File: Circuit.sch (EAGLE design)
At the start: 120 parts, among them IC1 LM1117T-3.3-V, U1 MAG3110, U10 MMA8452Q, U11 MMA8452Q, U12 MMA8452Q, U2 MAG3110, U3 L3G4200D, U4 L3G4200D, U5 L3G4200D, U6 L3G4200D, U7 MMA8452Q, U8 MMA8452Q, U9 MMA8452Q

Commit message: Corrected erc violations
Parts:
- C12, C7: value 4.7uF -> 10nF
- C15: value 2.2nF -> 470nF
- C16, C18, C43: value 0.1uF -> 2.2nF
- C17, C45: value 10nF -> 2.2nF
- C19, C2, C26, C33: value 4.7uF -> 0.1uF
- C22: value 2.2nF -> 4.7uF
- C23, C51: value 0.1uF -> 4.7uF
- C24, C49: value 10nF -> 4.7uF
- C29, C36, C9: value 2.2nF -> 10uF
- C30, C34, C35, C39, C57, C8: value 0.1uF -> 10nF
- C31: value 10nF -> 470nF
- C38, C41, C53: value 10nF -> 0.1uF
- C4: value 2.2nF -> 0.1uF
- C40, C48, C52: value 10uF -> 0.1uF
- C44: value 10uF -> 2.2nF
- C46, C54: value 470nF -> 0.1uF
- C50: value 470nF -> 4.7uF
- C56: value 0.1uF -> 10uF
- C58: value 0.1uF -> 470nF
- R1, R11, R2, R22, R26, R38: value 2.2K -> 10K
- R15, R18, R21, R24, R29, R30: value 10K -> 2.2K
- U$1: value RASPBERRY-PI_REV2 -> PCA9546A; device RaspberryPi:RASPBERRY-PI_REV2 -> Gyros:PCA9546A
- U$3: value PCA9546A -> RASPBERRY-PI_REV2; device Gyros:PCA9546A -> RaspberryPi:RASPBERRY-PI_REV2
- U12, U7, U8: value MMA8452Q -> L3G4200D; device SparkFun:MMA8452Q -> SparkFun:L3G4200D
- U4, U5, U6: value L3G4200D -> MMA8452Q; device SparkFun:L3G4200D -> SparkFun:MMA8452Q
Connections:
- net +3V3: now also C13.1, C14.1, C20.1, C21.1, C22.1, C29.1, C34.1, C35.1, C36.1, C46.1, C49.1, C5.1, C50.1, C56.1, C8.1, C9.1, ITG2.AD0, R1.1, R10.1, R12.1, R14.2, R15.2, R16.2, R17.2, R18.2, R19.2, R2.1, R21.1, R24.1, R25.1, R27.1, R28.1, R30.2, R31.2, R32.2, R35.2, R39.2, R40.2, R7.1, R8.1, R9.1, U$1.A2, U$1.VCC, U12.CS, U12.RSVDV@0, U12.SDO, U7.CS, U7.RSVDV@0, U7.SDO, U8.CS, U8.RSVDV@0; no longer C1.1, C11.1, C12.1, C15.2, C16.1, C16.2, C17.1, C18.1, C2.1, C22.2, C23.2, C26.1, C29.2, C30.1, C30.2, C31.1, C33.1, C38.1, C39.1, C43.1, C44.1, C6.1, ITG1.GND, ITG2.GND, ITG3.AD0, ITG3.GND, R1.2, R10.2, R11.2, R12.2, R14.1, R16.1, R17.1, R19.1, R2.2, R22.1, R25.2, R26.2, R27.2, R28.2, R30.1, R31.1, R32.1, R35.1, R38.1, R39.1, R40.1, R7.2, R8.2, R9.2, U$3.A2, U$3.VCC, U4.CS, U4.RSVDV@0, U4.SDO, U5.CS, U5.RSVDV@0, U6.CS, U6.RSVDV@0, U6.SDO
- net B1_SC0: now also R9.2, U$1.SC0; no longer R32.2, U$2.SC0
- net B1_SC1: now also ITG2.SCL, R8.2, U$1.SC1; no longer ITG3.SCL, R38.2, U$2.SC1
- net B1_SC2: now also R5.1, U$1.SC2, U7.SCL; no longer R28.1, U$2.SC2, U4.SCL
- net B1_SD0: now also R7.2, U$1.SD0; no longer R31.2, U$2.SD0
- net B1_SD1: now also ITG2.SDA, R10.2, R12.2, U$1.SD1; no longer ITG3.SDA, R14.2, R37.2, U$2.SD1
- net B1_SD2: now also R3.1, U$1.SD2, U7.SDA/SDI; no longer R27.1, U$2.SD2, U4.SDA/SDI
- net B2_SC0: now also ITG3.SCL, R28.2, U$2.SC0; no longer ITG2.SCL, R36.2, U$3.SC0
- net B2_SC1: now also R24.2, R29.2, U$2.SC1, U8.SCL; no longer R19.2, R40.2, U$3.SC1, U5.SCL
- net B2_SC2: now also R36.2, R6.1, U$2.SC2, U12.SCL; no longer R22.2, R26.1, U$3.SC2, U6.SCL
- net B2_SD0: now also ITG3.SDA, R23.2, U$2.SD0; no longer ITG2.SDA, R35.2, U$3.SD0
- net B2_SD1: now also R25.2, R27.2, U$2.SD1, U8.SDA/SDI; no longer R20.2, R39.2, U$3.SD1, U5.SDA/SDI
- net B2_SD2: now also R37.2, R4.1, U$2.SD2, U12.SDA/SDI; no longer R23.2, R25.1, U$3.SD2, U6.SDA/SDI
- net CLK1: now also R20.2, U$1.SCL, U$3.GPIO3,I2C0_SCL; no longer R16.2, U$1.GPIO3,I2C0_SCL, U$2.SCL
- net CLK2: now also U$2.SCL; no longer U$3.SCL
- net GND: now also C16.2, C22.2, C23.2, C29.2, C30.2, C46.2, C50.2, C54.2, ITG1.GND, ITG2.GND, ITG3.AD0, ITG3.GND, R11.1, R22.1, R26.1, R38.1, U$1.A0, U$1.A1, U$1.GND, U$3.GND@9, U12.GND, U12.RSDVG@3, U12.RSVDG@0, U12.RSVDG@1, U12.RSVDG@2, U12.RSVDG@4, U4.GND@0, U4.GND@1, U4.GND@2, U4.SA0, U5.GND@0, U5.GND@1, U5.GND@2, U5.SA0, U6.GND@0, U6.GND@1, U6.GND@2, U6.SA0, U7.GND, U7.RSDVG@3, U7.RSVDG@0, U7.RSVDG@1, U7.RSVDG@2, U7.RSVDG@4, U8.GND, U8.RSDVG@3, U8.RSVDG@0, U8.RSVDG@1, U8.RSVDG@2, U8.RSVDG@4, U8.SDO; no longer C31.2, C58.2, ITG2.AD0, R15.1, R18.1, R21.1, R24.1, U$1.GND@9, U$3.A0, U$3.A1, U$3.GND, U12.GND@0, U12.GND@1, U12.GND@2, U12.SA0, U4.GND, U4.RSDVG@3, U4.RSVDG@0, U4.RSVDG@1, U4.RSVDG@2, U4.RSVDG@4, U5.GND, U5.RSDVG@3, U5.RSVDG@0, U5.RSVDG@1, U5.RSVDG@2, U5.RSVDG@4, U5.SDO, U6.GND, U6.RSDVG@3, U6.RSVDG@0, U6.RSVDG@1, U6.RSVDG@2, U6.RSVDG@4, U7.GND@0, U7.GND@1, U7.GND@2, U7.SA0, U8.GND@0, U8.GND@1, U8.GND@2, U8.SA0
- net I1_AUXCLK: now also U5.SCL; no longer U7.SCL
- net I1_AUXSDA: now also U5.SDA; no longer U7.SDA
- net I2_AUXCLK: now also ITG3.AUX_CL, U10.SCL; no longer ITG2.AUX_CL, U8.SCL
- net I2_AUXSDA: now also ITG3.AUX_DA, U10.SDA; no longer ITG2.AUX_DA, U8.SDA
- net I2_INT: now also ITG3.INT; no longer ITG2.INT
- net I3_AUXCLK: now also ITG2.AUX_CL, U6.SCL; no longer ITG3.AUX_CL, U10.SCL
- net I3_AUXSDA: now also ITG2.AUX_DA, U6.SDA; no longer ITG3.AUX_DA, U10.SDA
- net I3_INT: now also ITG2.INT; no longer ITG3.INT
- net I4_AUXCLK: now also U11.SCL; no longer U12.SCL
- net I4_AUXSDA: now also U11.SDA; no longer U12.SDA
- net M1_AUXCLK: now also R14.1, U4.SCL; no longer R1.1, U9.SCL
- net M1_AUXSDA: now also R17.1, U4.SDA; no longer R2.1, U9.SDA
- net M2_AUXCLK: now also R30.1, U9.SCL; no longer R3.1, U11.SCL
- net M2_AUXSDA: now also R33.1, U9.SDA; no longer R4.1, U11.SDA
- net N$1: now also C16.1; no longer C4.1
- net N$10: now also U$3.5V@2; no longer U$1.5V@2
- net N$11: now also R15.1; no longer R5.1
- net N$12: now also R18.1; no longer R6.1
- net N$13: now also C10.1; no longer C14.1
- net N$14: now also C17.1; no longer C15.1
- net N$15: now also C54.1, U10.BYP; no longer C20.1, U8.BYP
- net N$16: now also R2.2, U$2.RESET; no longer R30.2, U$3.RESET
- net N$17: now also U$3.GND@14; no longer U$1.GND@14
- net N$18: now also R31.1; no longer R7.1
- net N$19: now also R34.1; no longer R8.1
- net N$2: now also C6.1; no longer C5.1
- net N$20: now also C37.1, ITG3.REGOUT; no longer C21.1, ITG2.REGOUT
- net N$21: now also C44.1, ITG3.CPOUT; no longer C22.1, ITG2.CPOUT
- net N$23: now also C28.1, U6.BYP; no longer C27.1, U10.BYP
- net N$24: now also C41.1; no longer C37.1
- net N$25: now also R16.1; no longer R9.1
- net N$26: now also R19.1; no longer R10.1
- net N$27: now also C11.1, ITG2.REGOUT; no longer C28.1, ITG3.REGOUT
- net N$28: now also C18.1, ITG2.CPOUT; no longer C29.1, ITG3.CPOUT
- net N$3: now also C26.1, U4.BYP; no longer C3.1, U9.BYP
- net N$30: now also C55.1, U11.BYP; no longer C34.1, U12.BYP
- net N$32: now also R32.1; no longer R11.1
- net N$33: now also R35.1; no longer R12.1
- net N$34: now also C38.1; no longer C35.1
- net N$35: now also C45.1; no longer C36.1
- net N$36: now also C30.1, C31.1, U7.PLL; no longer C45.1, C46.1, U4.PLL
- net N$38: now also C2.1; no longer C55.1
- net N$39: now also C12.1, C15.1; no longer C41.1, C42.1
- net N$40: now also C15.2, R11.2; no longer C42.2, R15.2
- net N$41: now also C31.2, R22.2; no longer C46.2, R18.2
- net N$42: now also R1.2, U$1.RESET; no longer R29.2, U$2.RESET
- net N$45: now also C39.1, C42.1, U8.PLL; no longer C49.1, C50.1, U5.PLL
- net N$46: now also C42.2, R26.2; no longer C50.2, R21.2
- net N$49: now also C4.1; no longer C56.1
- net N$5: now also C53.1, U9.BYP; no longer C8.1, U11.BYP
- net N$50: now also C57.1, C58.1, U12.PLL; no longer C53.1, C54.1, U6.PLL
- net N$51: now also C58.2, R38.2; no longer C54.2, R24.2
- net N$52: now also C1.1; no longer C57.1
- net N$53: now also C3.1; no longer C58.1
- net N$6: now also C43.1; no longer C9.1
- net N$7: now also C33.1; no longer C10.1
- net N$9: now also C27.1, U5.BYP; no longer C13.1, U7.BYP
- net SCL2: now also R40.1, U$3.GPIO29; no longer R34.1, U$1.GPIO29
- net SDA1: now also R21.2, U$1.SDA, U$3.GPIO2,I2C0_SDA; no longer R17.2, U$1.GPIO2,I2C0_SDA, U$2.SDA
- net SDA2: now also R39.1, U$2.SDA, U$3.GPIO28; no longer R33.1, U$1.GPIO28, U$3.SDA
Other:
- moved on the sheet: C1, C10, C11, C12, C13, C14, C15, C16, C17, C18, C19, C2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

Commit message: Finalises packages, adds labels to homemade stuff
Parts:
- C1, C10, C11, C12, C13, C14, C15, C16, C17, C18, C19, C2, C20, C21, C22, C23, C24, C25, C26, C27, C28, C29, C3, C30, C31, C32, C33, C34, C35, C36, C37, C38, C39, C4, C40, C41, C42, C43, C44, C45, C46, C47, C48, C49, C5, C50, C51, C52, C53, C54, C55, C56, C57, C58, C6, C7, C8, C9: device SparkFun:CAP0402-CAP -> SparkFun:CAP0603-CAP
- R1, R10, R11, R12, R13, R14, R15, R16, R17, R18, R19, R2, R20, R21, R22, R23, R24, R25, R26, R27, R28, R29, R3, R30, R31, R32, R33, R34, R35, R36, R37, R38, R39, R4, R40, R5, R6, R7, R8, R9: device resistor:R-EU_0207/10 -> resistor:R-EU_R0603
- renumbered U10 to ACL_4, U11 to ACL_6, U4 to ACL_1, U5 to ACL_3, U6 to ACL_5, U9 to ACL_2
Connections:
- net +3V3: now also ITG3.AD0; no longer ITG2.AD0
- net B1_SC1: now also ITG3.SCL; no longer ITG2.SCL
- net B1_SD1: now also ITG3.SDA; no longer ITG2.SDA
- net B2_SC0: now also ITG2.SCL; no longer ITG3.SCL
- net B2_SD0: now also ITG2.SDA; no longer ITG3.SDA
- net GND: now also ITG2.AD0; no longer ITG3.AD0
- net I2_AUXCLK: now also ITG2.AUX_CL; no longer ITG3.AUX_CL
- net I2_AUXSDA: now also ITG2.AUX_DA; no longer ITG3.AUX_DA
- net I2_INT: now also ITG2.INT; no longer ITG3.INT
- net I3_AUXCLK: now also ITG3.AUX_CL; no longer ITG2.AUX_CL
- net I3_AUXSDA: now also ITG3.AUX_DA; no longer ITG2.AUX_DA
- net I3_INT: now also ITG3.INT; no longer ITG2.INT
- net N$20: now also ITG2.REGOUT; no longer ITG3.REGOUT
- net N$21: now also ITG2.CPOUT; no longer ITG3.CPOUT
- net N$27: now also ITG3.REGOUT; no longer ITG2.REGOUT
- net N$28: now also ITG3.CPOUT; no longer ITG2.CPOUT
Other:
- moved on the sheet: ITG2, ITG3

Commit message: Placed test pads
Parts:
- added _B1_C0, _B1_C1, _B1_C2, _B1_D0, _B1_D2, _B1_SD1, _B2_C0, _B2_C1, _B2_C2, _B2_D0, _B2_D1, _B2_D2: TPB1,27, testpad:TPB1,27
- renumbered U12 to L3G_4, U3 to L3G_1, U7 to L3G_2, U8 to L3G_3
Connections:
- net B1_SC0: now also _B1_C0.TP
- net B1_SC1: now also _B1_C1.TP
- net B1_SC2: now also _B1_C2.TP
- net B1_SD0: now also _B1_D0.TP
- net B1_SD1: now also _B1_SD1.TP
- net B1_SD2: now also _B1_D2.TP
- net B2_SC0: now also _B2_C0.TP
- net B2_SC1: now also _B2_C1.TP
- net B2_SC2: now also _B2_C2.TP
- net B2_SD0: now also _B2_D0.TP
- net B2_SD1: now also _B2_D1.TP
- net B2_SD2: now also _B2_D2.TP

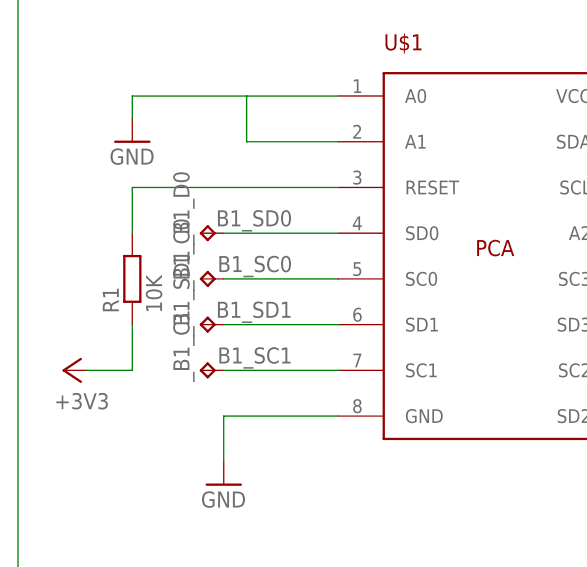
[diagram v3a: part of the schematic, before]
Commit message: Initial board layout complete
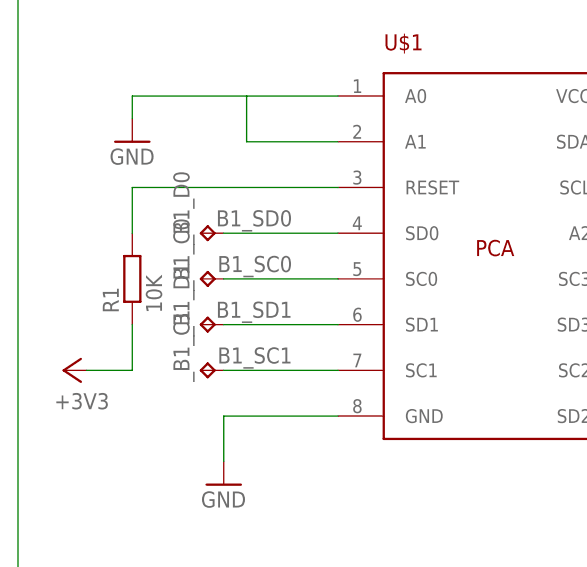
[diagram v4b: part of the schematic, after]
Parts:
- renumbered _B1_SD1 to _B1_D1
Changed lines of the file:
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@@
 <part name="_B1_D0" library="testpad" deviceset="TP" device="B1,27"/>
 <part name="_B1_C0" library="testpad" deviceset="TP" device="B1,27"/>
-<part name="_B1_SD1" library="testpad" deviceset="TP" device="B1,27"/>
+<part name="_B1_D1" library="testpad" deviceset="TP" device="B1,27"/>
 <part name="_B1_C1" library="testpad" deviceset="TP" device="B1,27"/>
 <part name="_B1_C2" library="testpad" deviceset="TP" device="B1,27"/>
@@
 <instance part="_B1_D0" gate="G$1" x="-198.12" y="325.12" rot="R90"/>
 <instance part="_B1_C0" gate="G$1" x="-198.12" y="320.04" rot="R90"/>
-<instance part="_B1_SD1" gate="G$1" x="-198.12" y="314.96" rot="R90"/>
+<instance part="_B1_D1" gate="G$1" x="-198.12" y="314.96" rot="R90"/>
 <instance part="_B1_C1" gate="G$1" x="-198.12" y="309.88" rot="R90"/>
 <instance part="_B1_C2" gate="G$1" x="-132.08" y="309.88" rot="R270"/>
@@
 <wire x1="-182.88" y1="314.96" x2="-195.58" y2="314.96" width="0.1524" layer="91"/>
 <label x="-187.96" y="317.5" size="1.778" layer="95" rot="R180"/>
-<pinref part="_B1_SD1" gate="G$1" pin="TP"/>
-</segment>
-<segment>
+<pinref part="_B1_D1" gate="G$1" pin="TP"/>
+</segment>
+<segment>

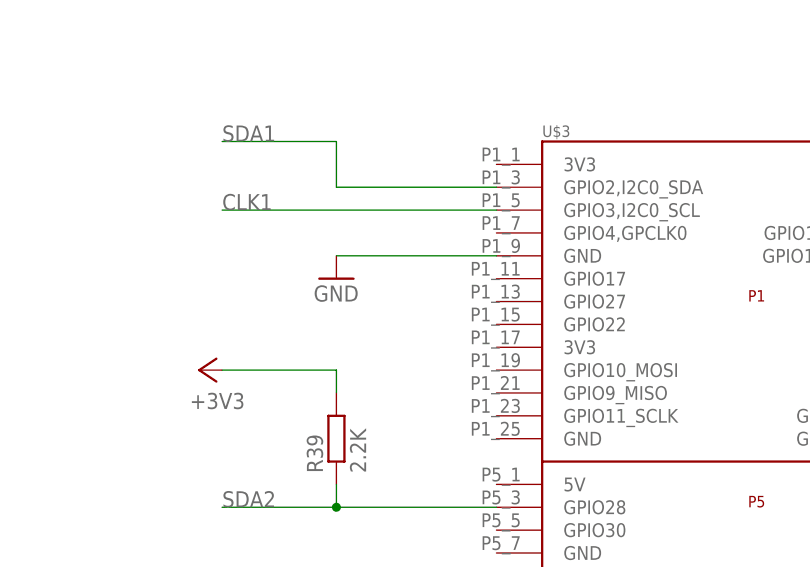
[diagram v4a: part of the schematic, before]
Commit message: Corrected GND connection
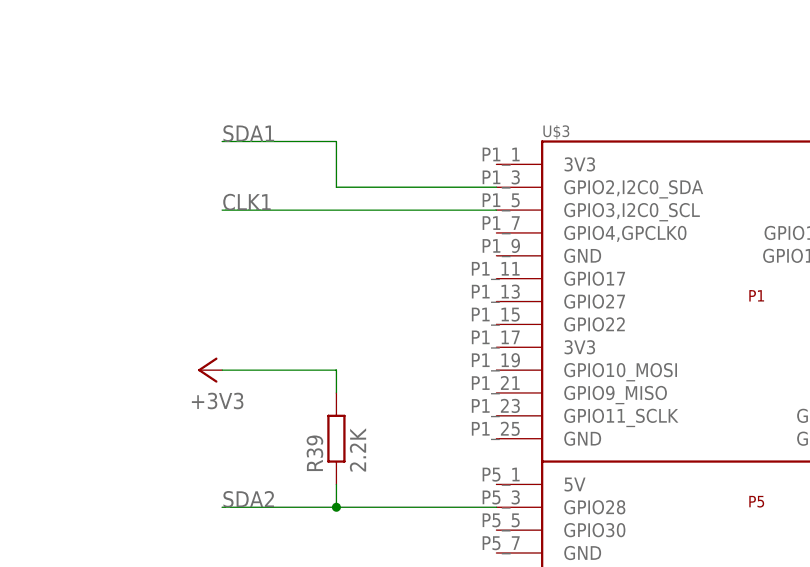
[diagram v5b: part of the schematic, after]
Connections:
- removed net N$17: IC1.GND, U$3.GND@14
- net GND: now also IC1.GND, U$3.GND@14; no longer U$3.GND@9
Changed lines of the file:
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@@
 <grid distance="0.1" unitdist="inch" unit="inch" style="lines" multiple="1" display="no" altdistance="0.01" altunitdist="inch" altunit="inch"/>
 <layers>
-<layer number="1" name="Top" color="4" fill="1" visible="yes" active="no"/>
-<layer number="16" name="Bottom" color="1" fill="1" visible="yes" active="no"/>
-<layer number="17" name="Pads" color="2" fill="1" visible="yes" active="no"/>
-<layer number="18" name="Vias" color="2" fill="1" visible="yes" active="no"/>
-<layer number="19" name="Unrouted" color="6" fill="1" visible="yes" active="no"/>
-<layer number="20" name="Dimension" color="15" fill="1" visible="yes" active="no"/>
-<layer number="21" name="tPlace" color="7" fill="1" visible="yes" active="no"/>
-<layer number="22" name="bPlace" color="7" fill="1" visible="yes" active="no"/>
-<layer number="23" name="tOrigins" color="15" fill="1" visible="yes" active="no"/>
-<layer number="24" name="bOrigins" color="15" fill="1" visible="yes" active="no"/>
-<layer number="25" name="tNames" color="7" fill="1" visible="yes" active="no"/>
-<layer number="26" name="bNames" color="7" fill="1" visible="yes" active="no"/>
-<layer number="27" name="tValues" color="7" fill="1" visible="yes" active="no"/>
-<layer number="28" name="bValues" color="7" fill="1" visible="yes" active="no"/>
+<layer number="1" name="Top" color="4" fill="1" visible="no" active="no"/>
+<layer number="16" name="Bottom" color="1" fill="1" visible="no" active="no"/>
+<layer number="17" name="Pads" color="2" fill="1" visible="no" active="no"/>
+<layer number="18" name="Vias" color="2" fill="1" visible="no" active="no"/>
+<layer number="19" name="Unrouted" color="6" fill="1" visible="no" active="no"/>
+<layer number="20" name="Dimension" color="15" fill="1" visible="no" active="no"/>
+<layer number="21" name="tPlace" color="7" fill="1" visible="no" active="no"/>
+<layer number="22" name="bPlace" color="7" fill="1" visible="no" active="no"/>
+<layer number="23" name="tOrigins" color="15" fill="1" visible="no" active="no"/>
+<layer number="24" name="bOrigins" color="15" fill="1" visible="no" active="no"/>
+<layer number="25" name="tNames" color="7" fill="1" visible="no" active="no"/>
+<layer number="26" name="bNames" color="7" fill="1" visible="no" active="no"/>
+<layer number="27" name="tValues" color="7" fill="1" visible="no" active="no"/>
+<layer number="28" name="bValues" color="7" fill="1" visible="no" active="no"/>
 <layer number="29" name="tStop" color="7" fill="3" visible="no" active="no"/>
 <layer number="30" name="bStop" color="7" fill="6" visible="no" active="no"/>
@@
 <layer number="35" name="tGlue" color="7" fill="4" visible="no" active="no"/>
 <layer number="36" name="bGlue" color="7" fill="5" visible="no" active="no"/>
-<layer number="37" name="tTest" color="7" fill="1" visible="yes" active="no"/>
-<layer number="38" name="bTest" color="7" fill="1" visible="yes" active="no"/>
+<layer number="37" name="tTest" color="7" fill="1" visible="no" active="no"/>
+<layer number="38" name="bTest" color="7" fill="1" visible="no" active="no"/>
 <layer number="39" name="tKeepout" color="4" fill="11" visible="no" active="no"/>
 <layer number="40" name="bKeepout" color="1" fill="11" visible="no" active="no"/>
@@
 <layer number="44" name="Drills" color="7" fill="1" visible="no" active="no"/>
 <layer number="45" name="Holes" color="7" fill="1" visible="no" active="no"/>
-<layer number="46" name="Milling" color="3" fill="1" visible="yes" active="no"/>
-<layer number="47" name="Measures" color="7" fill="1" visible="yes" active="no"/>
-<layer number="48" name="Document" color="7" fill="1" visible="yes" active="no"/>
-<layer number="49" name="Reference" color="7" fill="1" visible="yes" active="no"/>
-<layer number="50" name="dxf" color="7" fill="1" visible="yes" active="no"/>
-<layer number="51" name="tDocu" color="7" fill="1" visible="yes" active="no"/>
-<layer number="52" name="bDocu" color="7" fill="1" visible="yes" active="no"/>
-<layer number="53" name="tGND_GNDA" color="7" fill="1" visible="yes" active="no"/>
-<layer number="54" name="bGND_GNDA" color="7" fill="1" visible="yes" active="no"/>
-<layer number="56" name="wert" color="7" fill="1" visible="yes" active="no"/>
+<layer number="46" name="Milling" color="3" fill="1" visible="no" active="no"/>
+<layer number="47" name="Measures" color="7" fill="1" visible="no" active="no"/>
+<layer number="48" name="Document" color="7" fill="1" visible="no" active="no"/>
+<layer number="49" name="Reference" color="7" fill="1" visible="no" active="no"/>
+<layer number="50" name="dxf" color="7" fill="1" visible="no" active="no"/>
+<layer number="51" name="tDocu" color="7" fill="1" visible="no" active="no"/>
+<layer number="52" name="bDocu" color="7" fill="1" visible="no" active="no"/>
+<layer number="53" name="tGND_GNDA" color="7" fill="1" visible="no" active="no"/>
+<layer number="54" name="bGND_GNDA" color="7" fill="1" visible="no" active="no"/>
+<layer number="56" name="wert" color="7" fill="1" visible="no" active="no"/>
 <layer number="91" name="Nets" color="2" fill="1" visible="yes" active="yes"/>
 <layer number="92" name="Busses" color="1" fill="1" visible="yes" active="yes"/>
@@
 <part name="ACL_1" library="SparkFun" deviceset="MMA8452Q" device=""/>
 <part name="GND1" library="supply1" deviceset="GND" device=""/>
-<part name="GND2" library="supply1" deviceset="GND" device=""/>
 <part name="C19" library="SparkFun" deviceset="CAP" device="0603-CAP" value="0.1uF"/>
 <part name="C22" library="SparkFun" deviceset="CAP" device="0603-CAP" value="4.7uF"/>
@@
 <instance part="ACL_1" gate="G$1" x="53.34" y="317.5"/>
 <instance part="GND1" gate="1" x="-17.78" y="289.56"/>
-<instance part="GND2" gate="1" x="375.92" y="180.34"/>
 <instance part="C19" gate="G$1" x="0" y="309.88"/>
 <instance part="C22" gate="G$1" x="10.16" y="309.88"/>
@@
 <net name="GND" class="0">
 <segment>
-<pinref part="GND2" gate="1" pin="GND"/>
-<pinref part="U$3" gate="G$1" pin="GND@9"/>
-<wire x1="375.92" y1="182.88" x2="393.7" y2="182.88" width="0.1524" layer="91"/>
-</segment>
-<segment>
 <pinref part="ACL_1" gate="G$1" pin="GND@2"/>
 <wire x1="43.18" y1="314.96" x2="27.94" y2="307.34" width="0.1524" layer="91"/>
@@
 <wire x1="-27.94" y1="106.68" x2="-12.7" y2="106.68" width="0.1524" layer="91"/>
 </segment>
+<segment>
+<pinref part="IC1" gate="G$1" pin="GND"/>
+<wire x1="472.44" y1="185.42" x2="472.44" y2="177.8" width="0.1524" layer="91"/>
+<pinref part="U$3" gate="G$1" pin="GND@14"/>
+<wire x1="472.44" y1="177.8" x2="449.58" y2="177.8" width="0.1524" layer="91"/>
+</segment>
 </net>
 <net name="CLK1" class="0">
@@
 </segment>
 </net>
-<net name="N$17" class="0">
-<segment>
-<pinref part="IC1" gate="G$1" pin="GND"/>
-<wire x1="472.44" y1="185.42" x2="472.44" y2="177.8" width="0.1524" layer="91"/>
-<pinref part="U$3" gate="G$1" pin="GND@14"/>
-<wire x1="472.44" y1="177.8" x2="449.58" y2="177.8" width="0.1524" layer="91"/>
-</segment>
-</net>
